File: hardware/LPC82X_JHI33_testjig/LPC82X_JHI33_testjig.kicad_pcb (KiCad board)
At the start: 2 copper layers, 38.8 x 23.5 mm, 85 parts, among them J1 LPC82XJHI33_LEFT, J2 LPC82XJHI33_RIGHT, J3 JTAG_2X05

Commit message: updates to paste aperatures, update versionnumber
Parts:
- D1: value LED -> RED
- N2: value 20190412 -> 20190514
- R3: value R_Small -> 1K
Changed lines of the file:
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@@
     (zones 0)
     (modules 85)
-    (nets 57)
+    (nets 58)
   )
   (page A4)
@@
     (pad_to_mask_clearance 0.1)
     (solder_mask_min_width 0.1)
-    (pad_to_paste_clearance_ratio -0.1)
     (aux_axis_origin 0 0)
     (visible_elements FFFFFF7F)
@@
   (net 55 /Digital_stimulus)
   (net 56 "Net-(D1-Pad2)")
+  (net 57 "Net-(J3-Pad10)")
   (net_class Default "This is the default net class."
     (clearance 0.127)
@@
     (add_net "Net-(C9-Pad1)")
     (add_net "Net-(D1-Pad2)")
+    (add_net "Net-(J1-Pad15)")
+    (add_net "Net-(J1-Pad16)")
+    (add_net "Net-(J3-Pad10)")
     (add_net "Net-(J3-Pad2)")
     (add_net "Net-(J3-Pad4)")
+    (add_net "Net-(J3-Pad6)")
+    (add_net "Net-(J3-Pad7)")
+    (add_net "Net-(J3-Pad8)")
   )
   (module SquantorRcl:R_0402_hand (layer B.Cu)
@@
       (effects (font (size 1 1) (thickness 0.15)) (justify mirror))
     )
-    (fp_text value R_Small (at 0 -1.8 270) (layer B.Fab)
+    (fp_text value 1K (at 0 -1.8 270) (layer B.Fab)
       (effects (font (size 1 1) (thickness 0.15)) (justify mirror))
     )
@@
       (effects (font (size 1 1) (thickness 0.15)))
     )
-    (fp_text value LED (at 0 1.9 90) (layer F.Fab)
+    (fp_text value RED (at 0 1.9 90) (layer F.Fab)
       (effects (font (size 1 1) (thickness 0.15)))
     )
@@
       (effects (font (size 1 1) (thickness 0.15)) (justify mirror))
     )
-    (fp_text value 20190412 (at -0.4 0.137362 180) (layer B.SilkS)
+    (fp_text value 20190514 (at -0.4 0.137362 180) (layer B.SilkS)
       (effects (font (size 1 1) (thickness 0.15)) (justify mirror))
     )
@@
   (gr_line (start 108.3 94.9) (end 108.3 118.4) (layer Edge.Cuts) (width 0.15))
   (gr_line (start 69.5 94.9) (end 108.3 94.9) (layer Edge.Cuts) (width 0.15))
-  (segment (start 86.46 97.485) (end 86.46 97.51) (width 0.2) (layer F.Cu) (net 0))
-  (segment (start 86.45 97.495) (end 86.46 97.485) (width 0.2) (layer F.Cu) (net 0))
+  (segment (start 86.46 97.485) (end 86.46 97.51) (width 0.2) (layer F.Cu) (net 57))
+  (segment (start 86.45 97.495) (end 86.46 97.485) (width 0.2) (layer F.Cu) (net 57))
   (segment (start 93.45 101.8) (end 92.3 101.8) (width 0.2) (layer B.Cu) (net 1))
   (segment (start 92.25 105.7) (end 93.45 105.7) (width 0.2) (layer B.Cu) (net 2))

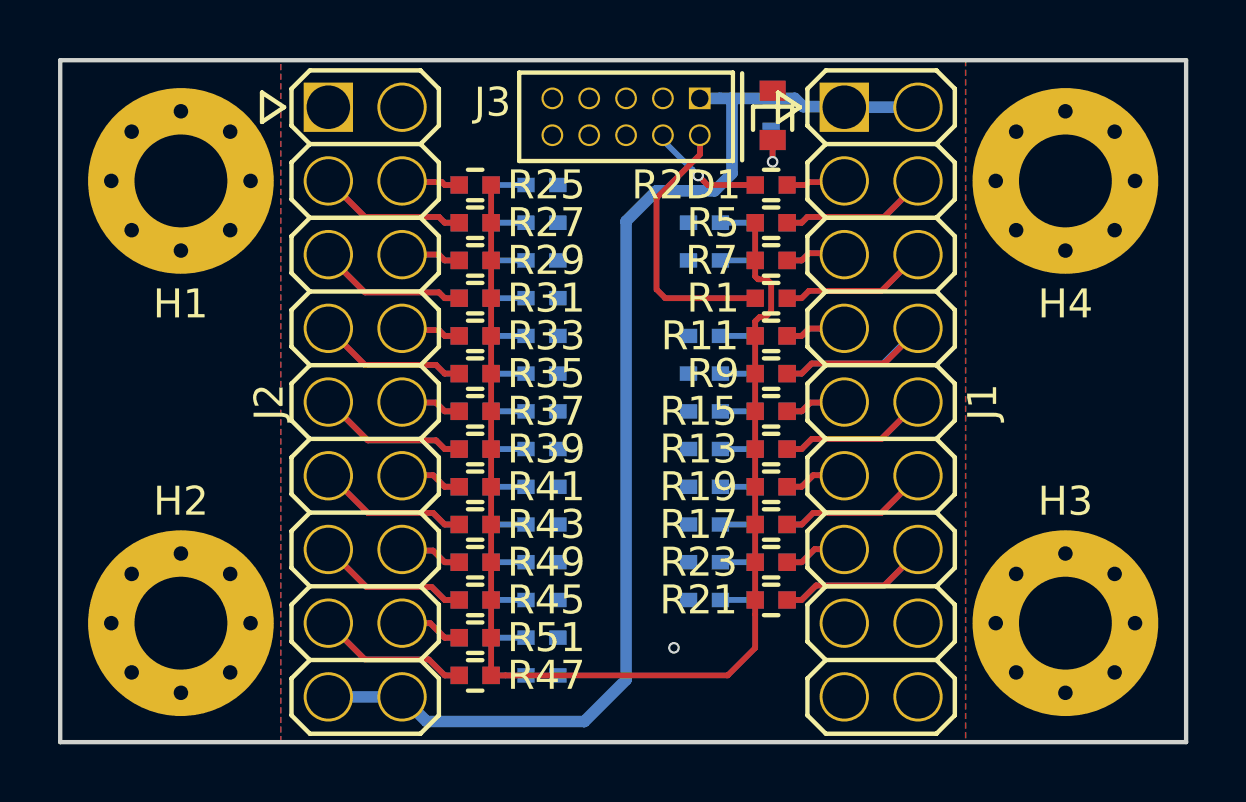
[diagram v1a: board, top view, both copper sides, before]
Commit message: fixed weird trace position
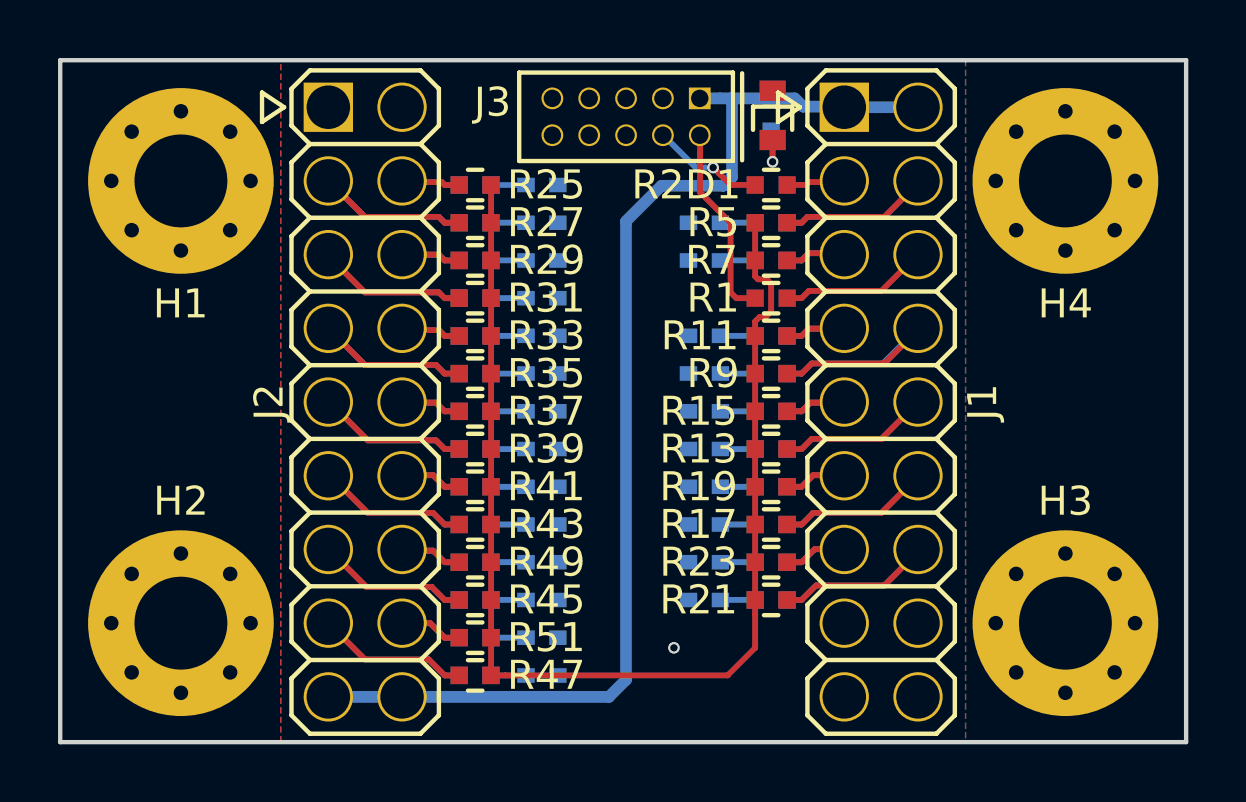
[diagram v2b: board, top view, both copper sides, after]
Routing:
- net Net-(J3-Pad2): track 9.45 -> 6.82 mm
- net /VDD: track 41.6 -> 41.0 mm
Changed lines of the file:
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@@
     (zones 0)
     (modules 85)
-    (nets 58)
+    (nets 57)
   )
   (page A4)
@@
   )
   (setup
-    (last_trace_width 0.127)
+    (last_trace_width 0.2)
     (user_trace_width 0.127)
     (user_trace_width 0.2)
@@
   (net 55 /Digital_stimulus)
   (net 56 "Net-(D1-Pad2)")
-  (net 57 "Net-(J3-Pad10)")
   (net_class Default "This is the default net class."
     (clearance 0.127)
@@
     (add_net "Net-(C9-Pad1)")
     (add_net "Net-(D1-Pad2)")
-    (add_net "Net-(J1-Pad15)")
-    (add_net "Net-(J1-Pad16)")
-    (add_net "Net-(J3-Pad10)")
     (add_net "Net-(J3-Pad2)")
     (add_net "Net-(J3-Pad4)")
-    (add_net "Net-(J3-Pad6)")
-    (add_net "Net-(J3-Pad7)")
-    (add_net "Net-(J3-Pad8)")
   )
   (module SquantorRcl:R_0402_hand (layer B.Cu)
@@
   (gr_line (start 108.3 94.9) (end 108.3 118.4) (layer Edge.Cuts) (width 0.15))
   (gr_line (start 69.5 94.9) (end 108.3 94.9) (layer Edge.Cuts) (width 0.15))
-  (segment (start 86.46 97.485) (end 86.46 97.51) (width 0.2) (layer F.Cu) (net 57))
-  (segment (start 86.45 97.495) (end 86.46 97.485) (width 0.2) (layer F.Cu) (net 57))
   (segment (start 93.45 101.8) (end 92.3 101.8) (width 0.2) (layer B.Cu) (net 1))
   (segment (start 92.25 105.7) (end 93.45 105.7) (width 0.2) (layer B.Cu) (net 2))
@@
   (segment (start 83.25 99.2) (end 82.75 99.2) (width 0.2) (layer B.Cu) (net 28))
   (segment (start 82.65 99.1) (end 81.3 99.1) (width 0.2) (layer B.Cu) (net 28))
-  (segment (start 93.45 103.1) (end 90.35 103.1) (width 0.2) (layer F.Cu) (net 29))
-  (segment (start 90.35 103.1) (end 90.05 102.8) (width 0.2) (layer F.Cu) (net 29))
-  (segment (start 90.05 102.8) (end 90.05 99.65) (width 0.2) (layer F.Cu) (net 29))
-  (segment (start 90.05 99.65) (end 91.55 98.15) (width 0.2) (layer F.Cu) (net 29))
-  (segment (start 91.55 98.15) (end 91.55 97.5) (width 0.2) (layer F.Cu) (net 29))
-  (segment (start 91.684926 99.072989) (end 91.484927 98.87299) (width 0.2) (layer F.Cu) (net 30))
-  (segment (start 90.3 97.688063) (end 91.284928 98.672991) (width 0.2) (layer B.Cu) (net 30))
-  (segment (start 91.284928 98.672991) (end 91.484927 98.87299) (width 0.2) (layer B.Cu) (net 30))
-  (segment (start 90.3 97.5) (end 90.3 97.688063) (width 0.2) (layer B.Cu) (net 30))
-  (segment (start 91.811937 99.2) (end 91.684926 99.072989) (width 0.2) (layer F.Cu) (net 30))
-  (segment (start 93.45 99.2) (end 91.811937 99.2) (width 0.2) (layer F.Cu) (net 30))
-  (via (at 91.484927 98.87299) (size 0.4) (drill 0.254) (layers F.Cu B.Cu) (net 30))
   (via (at 90.65 115.15) (size 0.4) (drill 0.254) (layers F.Cu B.Cu) (net 31))
   (segment (start 96.52 96.52) (end 99.03 96.52) (width 0.4) (layer B.Cu) (net 32))
@@
   (segment (start 92.235 96.215) (end 94.815 96.215) (width 0.4) (layer B.Cu) (net 32))
   (segment (start 91.54 96.215) (end 92.235 96.215) (width 0.4) (layer B.Cu) (net 32))
-  (segment (start 92.65 98.8) (end 92.65 96.2) (width 0.4) (layer B.Cu) (net 32))
-  (segment (start 92.05 99.4) (end 92.65 98.8) (width 0.4) (layer B.Cu) (net 32))
-  (segment (start 81.28 116.84) (end 82.129999 117.689999) (width 0.4) (layer B.Cu) (net 32))
-  (segment (start 82.129999 117.689999) (end 87.560001 117.689999) (width 0.4) (layer B.Cu) (net 32))
-  (segment (start 87.560001 117.689999) (end 89 116.25) (width 0.4) (layer B.Cu) (net 32))
-  (segment (start 89 116.25) (end 89 100.45) (width 0.4) (layer B.Cu) (net 32))
-  (segment (start 89 100.45) (end 90.05 99.4) (width 0.4) (layer B.Cu) (net 32))
-  (segment (start 90.05 99.4) (end 92.05 99.4) (width 0.4) (layer B.Cu) (net 32))
   (segment (start 92.25 100.5) (end 93.45 100.5) (width 0.2) (layer B.Cu) (net 33))
   (segment (start 92.25 104.4) (end 93.4 104.4) (width 0.2) (layer B.Cu) (net 34))
@@
   (segment (start 94.05 98.4) (end 94.05 97.4) (width 0.2) (layer B.Cu) (net 56))
   (segment (start 94.05 97.4) (end 94 97.35) (width 0.2) (layer B.Cu) (net 56))
+  (segment (start 86.46 97.485) (end 86.46 97.51) (width 0.2) (layer F.Cu) (net 0))
+  (segment (start 86.45 97.495) (end 86.46 97.485) (width 0.2) (layer F.Cu) (net 0))
+  (segment (start 91.55 98.15) (end 91.55 97.5) (width 0.2) (layer F.Cu) (net 29))
+  (segment (start 91.55 98.15) (end 91.55 99.45) (width 0.2) (layer F.Cu) (net 29))
+  (segment (start 91.55 99.45) (end 92.6 100.5) (width 0.2) (layer F.Cu) (net 29))
+  (segment (start 92.6 100.5) (end 92.6 102.9) (width 0.2) (layer F.Cu) (net 29))
+  (segment (start 92.6 102.9) (end 92.8 103.1) (width 0.2) (layer F.Cu) (net 29))
+  (segment (start 92.8 103.1) (end 93.5 103.1) (width 0.2) (layer F.Cu) (net 29))
+  (segment (start 91.4 98.6) (end 91.717158 98.6) (width 0.2) (layer B.Cu) (net 30))
+  (segment (start 93.45 99.2) (end 92.6 99.2) (width 0.2) (layer F.Cu) (net 30))
+  (segment (start 92.6 99.2) (end 92.199999 98.799999) (width 0.2) (layer F.Cu) (net 30))
+  (via (at 92 98.6) (size 0.4) (drill 0.254) (layers F.Cu B.Cu) (net 30))
+  (segment (start 92.199999 98.799999) (end 92 98.6) (width 0.2) (layer F.Cu) (net 30))
+  (segment (start 90.3 97.5) (end 91.4 98.6) (width 0.2) (layer B.Cu) (net 30))
+  (segment (start 91.717158 98.6) (end 92 98.6) (width 0.2) (layer B.Cu) (net 30))
+  (segment (start 81.28 116.84) (end 88.41 116.84) (width 0.4) (layer B.Cu) (net 32))
+  (segment (start 92.352943 99.227021) (end 92.65 98.929964) (width 0.4) (layer B.Cu) (net 32))
+  (segment (start 89 116.25) (end 89 100.45) (width 0.4) (layer B.Cu) (net 32))
+  (segment (start 90.222979 99.227021) (end 92.352943 99.227021) (width 0.4) (layer B.Cu) (net 32))
+  (segment (start 89 100.45) (end 90.222979 99.227021) (width 0.4) (layer B.Cu) (net 32))
+  (segment (start 92.65 98.929964) (end 92.65 96.2) (width 0.4) (layer B.Cu) (net 32))
+  (segment (start 88.41 116.84) (end 89 116.25) (width 0.4) (layer B.Cu) (net 32))
   (zone (net 31) (net_name /VSS) (layer B.Cu) (hatch edge 0.508)
     (connect_pads (clearance 0.3))
